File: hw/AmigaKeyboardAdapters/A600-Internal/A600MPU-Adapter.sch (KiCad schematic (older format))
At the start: 9 parts, among them P1 Conn_02x03_Odd_Even, P2 Conn_01x03_Male, U1 6571R4_PLCC44_MPUKEY_REV

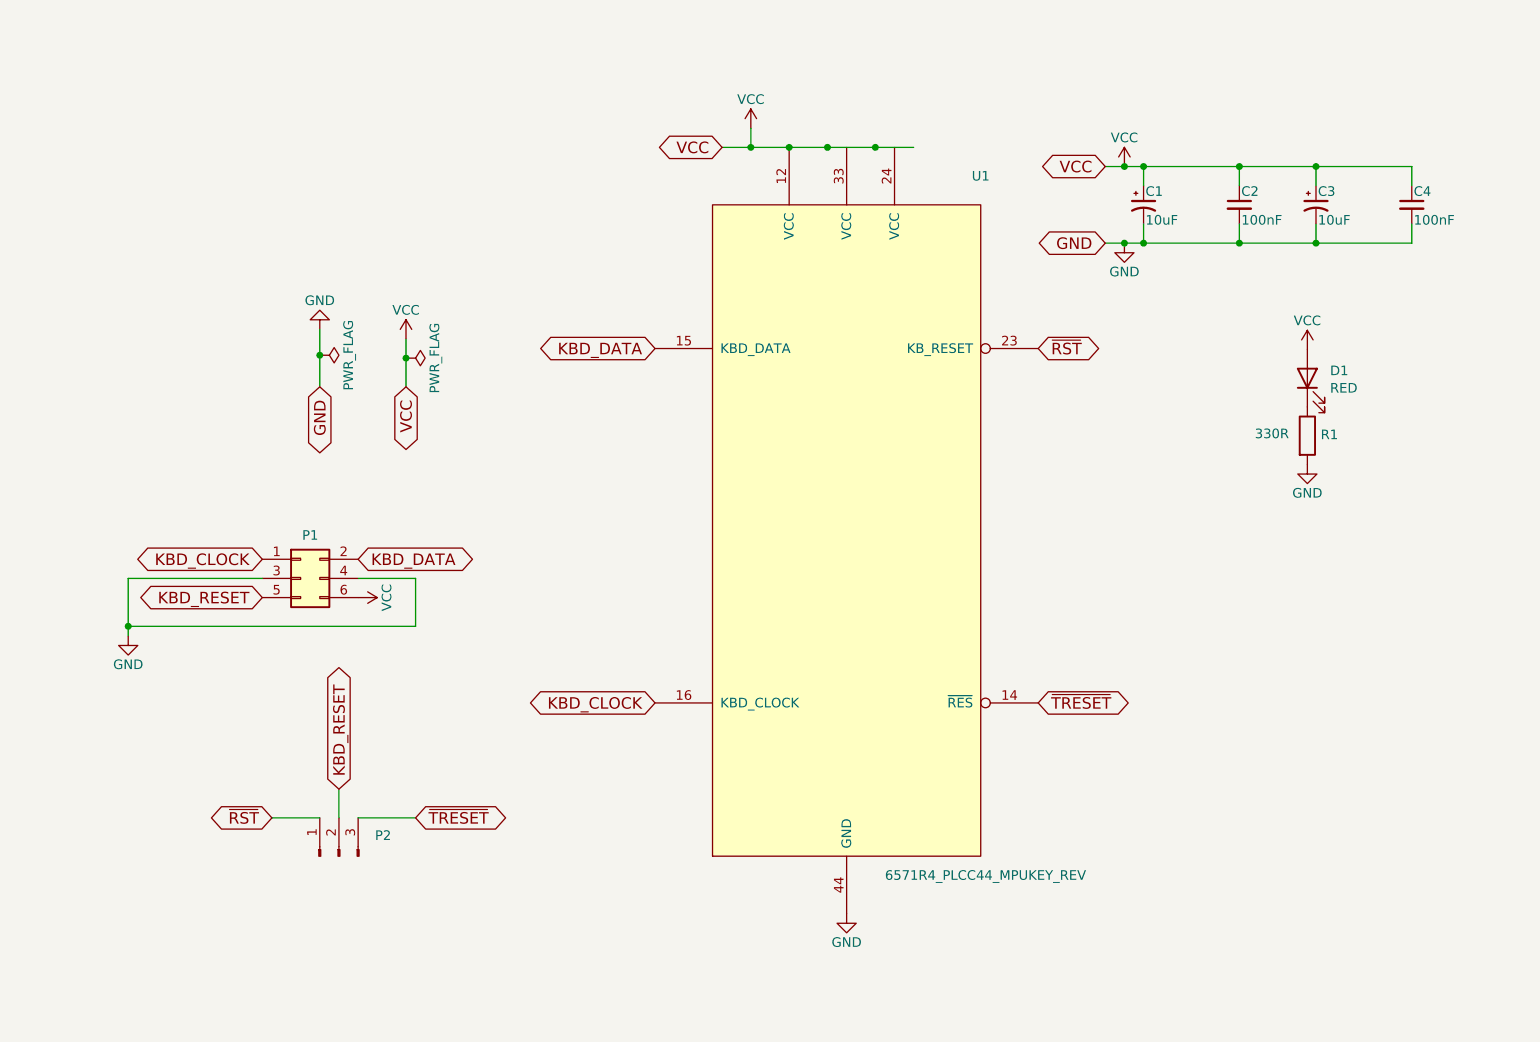
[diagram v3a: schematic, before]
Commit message: Updated the symbol and the positioning of the footprint in bottom layer. Now all signals are checked with PCBEXPLORER for A600 (June Bug version) They seem to be ok. Updated from library too.
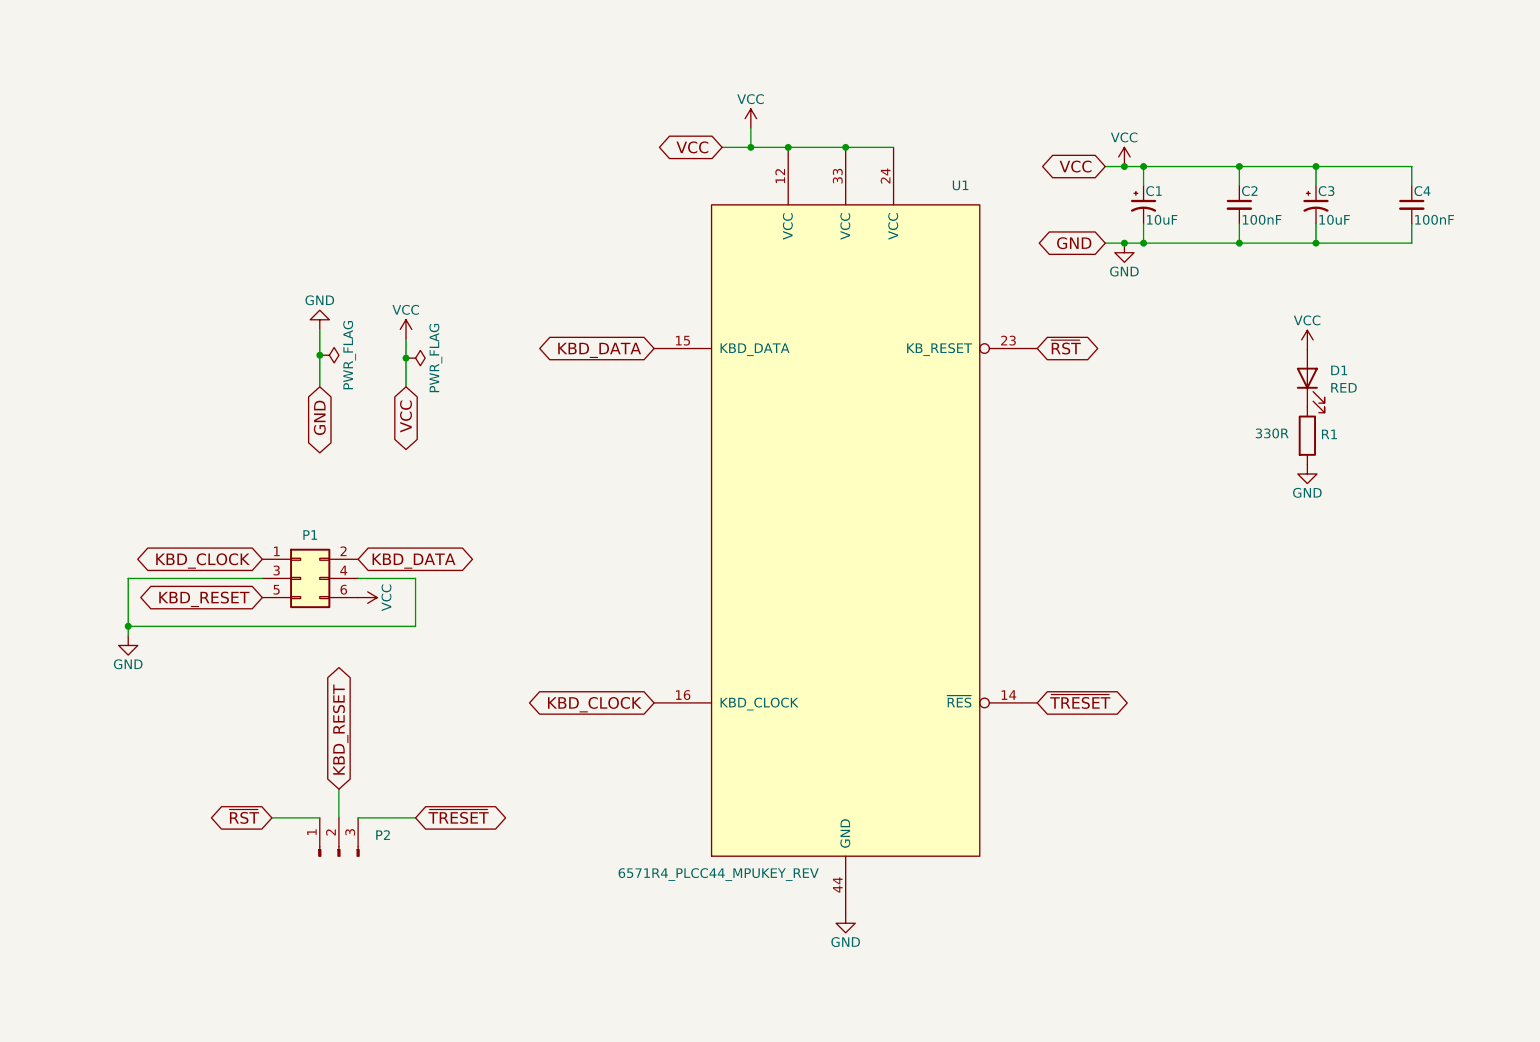
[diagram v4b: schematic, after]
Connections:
- wire segments 37 -> 36
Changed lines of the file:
@@
 Sheet 1 1
 Title "Amiga 600 MPU Keyboard Adapter"
-Date "2022-11-29"
-Rev "2.0"
+Date "2026-02-19"
+Rev "2.1"
 Comp "RetroBit Lab"
 Comment1 ""
@@
 Text GLabel 5700 1800 0    60   BiDi ~ 0
 VCC
-Text GLabel 7350 2850 2    60   BiDi ~ 0
+Text GLabel 7345 2850 2    60   BiDi ~ 0
 ~RST
-Text GLabel 5350 2850 0    60   BiDi ~ 0
+Text GLabel 5345 2850 0    60   BiDi ~ 0
 KBD_DATA
-Text GLabel 5350 4700 0    60   BiDi ~ 0
+Text GLabel 5345 4700 0    60   BiDi ~ 0
 KBD_CLOCK
-Text GLabel 7350 4700 2    60   BiDi ~ 0
+Text GLabel 7345 4700 2    60   BiDi ~ 0
 ~TRESET
 Wire Wire Line
@@
 $EndComp
 $Comp
+L power:GND #PWR04
+U 1 1 6388659D
+P 6345 5800
+F 0 "#PWR04" H 6345 5550 50  0001 C CNN
+F 1 "GND" H 6345 5650 50  0000 C CNN
+F 2 "" H 6345 5800 50  0001 C CNN
+F 3 "" H 6345 5800 50  0001 C CNN
+	1    6345 5800
+	1    0    0    -1
+$EndComp
+$Comp
 L RetroBitLab:6571R4_PLCC44_MPUKEY_REV U1
-U 1 1 5BECAC84
-P 6350 3800
-F 0 "U1" H 7050 5650 50  0000 C CNN
-F 1 "6571R4_PLCC44_MPUKEY_REV" H 6550 2000 50  0000 L CNN
-F 2 "RetroBitLab:PLCC-44_THT-Socket_3D" H 6350 3800 60  0001 C CNN
-F 3 "" H 6350 3800 60  0000 C CNN
-	1    6350 3800
-	1    0    0    -1
-$EndComp
-Wire Wire Line
-	5850 1800 6050 1800
-Wire Wire Line
-	6500 1800 6700 1800
-Wire Wire Line
-	6500 1800 6250 1800
-Connection ~ 6500 1800
-Wire Wire Line
-	6250 1800 6050 1800
-Connection ~ 6250 1800
-Connection ~ 6050 1800
-$Comp
-L power:GND #PWR?
-U 1 1 6388659D
-P 6350 5800
-F 0 "#PWR?" H 6350 5550 50  0001 C CNN
-F 1 "GND" H 6350 5650 50  0000 C CNN
-F 2 "" H 6350 5800 50  0001 C CNN
-F 3 "" H 6350 5800 50  0001 C CNN
-	1    6350 5800
-	1    0    0    -1
-$EndComp
+U 1 1 6996E811
+P 6345 3800
+F 0 "U1" H 6945 5600 50  0000 C CNN
+F 1 "6571R4_PLCC44_MPUKEY_REV" H 5680 2010 50  0000 C CNN
+F 2 "RetroBitLab:PLCC-44_THT-Socket_3D" H 6345 3800 60  0001 C CNN
+F 3 "" H 6345 3800 60  0000 C CNN
+	1    6345 3800
+	1    0    0    -1
+$EndComp
+Wire Wire Line
+	5850 1800 6045 1800
+Wire Wire Line
+	6045 1800 6345 1800
+Connection ~ 6045 1800
+Wire Wire Line
+	6345 1800 6595 1800
+Connection ~ 6345 1800
 $EndSCHEMATC
